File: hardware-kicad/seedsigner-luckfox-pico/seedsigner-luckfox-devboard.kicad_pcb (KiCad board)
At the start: 2 copper layers, 100 x 100 mm, 37 parts, among them J1 Conn_01x10, J2 Conn_01x05, U1 LuckFox_Pico, U2 RASPBERRY_PI_3_MODEL_B+

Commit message: export footprint library pretty files, and update pcb to use library
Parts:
- ART1: footprint SeedSigner:LightningSpore_Logo -> seedsigner-luckfox:LightningSpore_Logo
- C1: footprint Capacitor_THT:CP_Radial_D5.0mm_P2.50mm -> seedsigner-luckfox:CP_Radial_D5.0mm_P2.50mm
- H1, H2, H3, H4: footprint SeedSigner:MOUNT_HOLE_3MM -> seedsigner-luckfox:MOUNT_HOLE_3MM
- J1: footprint Connector_PinHeader_2.54mm:PinHeader_1x10_P2.54mm_Horizontal -> seedsigner-luckfox:PinHeader_1x10_P2.54mm_Horizontal
- J2: footprint Connector_PinHeader_2.54mm:PinHeader_1x05_P2.54mm_Horizontal -> seedsigner-luckfox:PinHeader_1x05_P2.54mm_Horizontal
- JP1: footprint Jumper:SolderJumper-2_P1.3mm_Bridged_Pad1.0x1.5mm -> seedsigner-luckfox:SolderJumper-2_P1.3mm_Bridged_Pad1.0x1.5mm
- JP2: footprint Jumper:SolderJumper-2_P1.3mm_Open_Pad1.0x1.5mm -> seedsigner-luckfox:SolderJumper-2_P1.3mm_Open_Pad1.0x1.5mm
- LOGO1: footprint SeedSigner:seedsigner-logo-small -> seedsigner-luckfox:seedsigner-logo-small
- LOGO2: footprint SeedSigner:corn-logo -> seedsigner-luckfox:corn-logo
- R1, R2, R3, R4, R5, R6, R7, R8: footprint Resistor_SMD:R_2512_6332Metric -> seedsigner-luckfox:R_2512_6332Metric
- TP1, TP10, TP11, TP12, TP13, TP14, TP15, TP2, TP3, TP4, TP5, TP6, TP7, TP8, TP9: footprint TestPoint:TestPoint_Pad_1.5x1.5mm -> seedsigner-luckfox:TestPoint_Pad_1.5x1.5mm
- U1: footprint SeedSigner:LUCKFOX_PICO_PRO_MAX_PTH -> seedsigner-luckfox:LUCKFOX_PICO_PRO_MAX_PTH
- U2: footprint SeedSigner:WAVESHARE_LCD_BUTTON -> seedsigner-luckfox:WAVESHARE_LCD_BUTTON
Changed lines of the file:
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@@
 	(net 54 "Net-(U1-GPIO4_C1_z)")
 	(net 55 "Net-(U1-GPIO0_A7_d)")
-	(footprint "TestPoint:TestPoint_Pad_1.5x1.5mm"
+	(footprint "seedsigner-luckfox:TestPoint_Pad_1.5x1.5mm"
 		(layer "F.Cu")
 		(at 59 15)
@@
 		)
 	)
-	(footprint "Resistor_SMD:R_2512_6332Metric"
+	(footprint "seedsigner-luckfox:R_2512_6332Metric"
 		(layer "F.Cu")
 		(at 17.8 50.2375 90)
@@
 		)
 	)
-	(footprint "TestPoint:TestPoint_Pad_1.5x1.5mm"
+	(footprint "seedsigner-luckfox:TestPoint_Pad_1.5x1.5mm"
 		(layer "F.Cu")
 		(at 40.75 15)
@@
 		)
 	)
-	(footprint "Capacitor_THT:CP_Radial_D5.0mm_P2.50mm"
+	(footprint "seedsigner-luckfox:CP_Radial_D5.0mm_P2.50mm"
 		(layer "F.Cu")
 		(at 71 53 180)
@@
 		)
 	)
-	(footprint "Resistor_SMD:R_2512_6332Metric"
+	(footprint "seedsigner-luckfox:R_2512_6332Metric"
 		(layer "F.Cu")
 		(at 32.2 50.2 90)
@@
 		)
 	)
-	(footprint "TestPoint:TestPoint_Pad_1.5x1.5mm"
+	(footprint "seedsigner-luckfox:TestPoint_Pad_1.5x1.5mm"
 		(layer "F.Cu")
 		(at 6.25 13.75)
@@
 		)
 	)
-	(footprint "SeedSigner:LightningSpore_Logo"
+	(footprint "seedsigner-luckfox:LightningSpore_Logo"
 		(layer "F.Cu")
 		(at 94.85827 53.012464 90)
@@
 		)
 	)
-	(footprint "SeedSigner:seedsigner-logo-small"
+	(footprint "seedsigner-luckfox:seedsigner-logo-small"
 		(layer "F.Cu")
 		(at 95.175 20.875 90)
@@
 		)
 	)
-	(footprint "Resistor_SMD:R_2512_6332Metric"
+	(footprint "seedsigner-luckfox:R_2512_6332Metric"
 		(layer "F.Cu")
 		(at 22.6 50.2 90)
@@
 		)
 	)
-	(footprint "Resistor_SMD:R_2512_6332Metric"
+	(footprint "seedsigner-luckfox:R_2512_6332Metric"
 		(layer "F.Cu")
 		(at 47 50.1625 90)
@@
 		)
 	)
-	(footprint "TestPoint:TestPoint_Pad_1.5x1.5mm"
+	(footprint "seedsigner-luckfox:TestPoint_Pad_1.5x1.5mm"
 		(layer "F.Cu")
 		(at 48.5 15)
@@
 		)
 	)
-	(footprint "Connector_PinHeader_2.54mm:PinHeader_1x05_P2.54mm_Horizontal"
+	(footprint "seedsigner-luckfox:PinHeader_1x05_P2.54mm_Horizontal"
 		(layer "F.Cu")
 		(at 63.675 11.375 90)
@@
 		)
 	)
-	(footprint "TestPoint:TestPoint_Pad_1.5x1.5mm"
+	(footprint "seedsigner-luckfox:TestPoint_Pad_1.5x1.5mm"
 		(layer "F.Cu")
 		(at 6.25 26.25)
@@
 		)
 	)
-	(footprint "TestPoint:TestPoint_Pad_1.5x1.5mm"
+	(footprint "seedsigner-luckfox:TestPoint_Pad_1.5x1.5mm"
 		(layer "F.Cu")
 		(at 55.75 41.5)
@@
 		)
 	)
-	(footprint "SeedSigner:MOUNT_HOLE_3MM"
+	(footprint "seedsigner-luckfox:MOUNT_HOLE_3MM"
 		(layer "F.Cu")
 		(at 95 5)
@@
 		)
 	)
-	(footprint "TestPoint:TestPoint_Pad_1.5x1.5mm"
+	(footprint "seedsigner-luckfox:TestPoint_Pad_1.5x1.5mm"
 		(layer "F.Cu")
 		(at 51.5 15)
@@
 		)
 	)
-	(footprint "Jumper:SolderJumper-2_P1.3mm_Open_Pad1.0x1.5mm"
+	(footprint "seedsigner-luckfox:SolderJumper-2_P1.3mm_Open_Pad1.0x1.5mm"
 		(layer "F.Cu")
 		(at 77.65 61.7 180)
@@
 		)
 	)
-	(footprint "Resistor_SMD:R_2512_6332Metric"
+	(footprint "seedsigner-luckfox:R_2512_6332Metric"
 		(layer "F.Cu")
 		(at 42 50.2 90)
@@
 		)
 	)
-	(footprint "TestPoint:TestPoint_Pad_1.5x1.5mm"
+	(footprint "seedsigner-luckfox:TestPoint_Pad_1.5x1.5mm"
 		(layer "F.Cu")
 		(at 54.25 15)
@@
 		)
 	)
-	(footprint "SeedSigner:WAVESHARE_LCD_BUTTON"
+	(footprint "seedsigner-luckfox:WAVESHARE_LCD_BUTTON"
 		(layer "F.Cu")
 		(at 49 83.8 180)
@@
 		)
 	)
-	(footprint "Resistor_SMD:R_2512_6332Metric"
+	(footprint "seedsigner-luckfox:R_2512_6332Metric"
 		(layer "F.Cu")
 		(at 27.4 50.2 90)
@@
 		)
 	)
-	(footprint "SeedSigner:MOUNT_HOLE_3MM"
+	(footprint "seedsigner-luckfox:MOUNT_HOLE_3MM"
 		(layer "F.Cu")
 		(at 95 95)
@@
 		)
 	)
-	(footprint "TestPoint:TestPoint_Pad_1.5x1.5mm"
+	(footprint "seedsigner-luckfox:TestPoint_Pad_1.5x1.5mm"
 		(layer "F.Cu")
 		(at 38.25 15)
@@
 		)
 	)
-	(footprint "SeedSigner:LUCKFOX_PICO_PRO_MAX_PTH"
+	(footprint "seedsigner-luckfox:LUCKFOX_PICO_PRO_MAX_PTH"
 		(layer "F.Cu")
 		(at 17.86 36.5 90)
@@
 		)
 	)
-	(footprint "SeedSigner:corn-logo"
+	(footprint "seedsigner-luckfox:corn-logo"
 		(layer "F.Cu")
 		(at 93.056841 83.1 90)
@@
 		)
 	)
-	(footprint "Resistor_SMD:R_2512_6332Metric"
+	(footprint "seedsigner-luckfox:R_2512_6332Metric"
 		(layer "F.Cu")
 		(at 37 50.2 90)
@@
 		)
 	)
-	(footprint "TestPoint:TestPoint_Pad_1.5x1.5mm"
+	(footprint "seedsigner-luckfox:TestPoint_Pad_1.5x1.5mm"
 		(layer "F.Cu")
 		(at 6.25 17.75)
@@
 		)
 	)
-	(footprint "TestPoint:TestPoint_Pad_1.5x1.5mm"
+	(footprint "seedsigner-luckfox:TestPoint_Pad_1.5x1.5mm"
 		(layer "F.Cu")
 		(at 33.25 15)
@@
 		)
 	)
-	(footprint "TestPoint:TestPoint_Pad_1.5x1.5mm"
+	(footprint "seedsigner-luckfox:TestPoint_Pad_1.5x1.5mm"
 		(layer "F.Cu")
 		(at 61.75 15)
@@
 		)
 	)
-	(footprint "Jumper:SolderJumper-2_P1.3mm_Bridged_Pad1.0x1.5mm"
+	(footprint "seedsigner-luckfox:SolderJumper-2_P1.3mm_Bridged_Pad1.0x1.5mm"
 		(layer "F.Cu")
 		(at 74.15 61.7)
@@
 		)
 	)
-	(footprint "Connector_PinHeader_2.54mm:PinHeader_1x10_P2.54mm_Horizontal"
+	(footprint "seedsigner-luckfox:PinHeader_1x10_P2.54mm_Horizontal"
 		(layer "F.Cu")
 		(at 10 77.5 180)
@@
 		)
 	)
-	(footprint "TestPoint:TestPoint_Pad_1.5x1.5mm"
+	(footprint "seedsigner-luckfox:TestPoint_Pad_1.5x1.5mm"
 		(layer "F.Cu")
 		(at 6.25 22)
@@
 		)
 	)
-	(footprint "SeedSigner:MOUNT_HOLE_3MM"
+	(footprint "seedsigner-luckfox:MOUNT_HOLE_3MM"
 		(layer "F.Cu")
 		(at 5 5)
@@
 		)
 	)
-	(footprint "TestPoint:TestPoint_Pad_1.5x1.5mm"
+	(footprint "seedsigner-luckfox:TestPoint_Pad_1.5x1.5mm"
 		(layer "F.Cu")
 		(at 44.75 15)
@@
 		)
 	)
-	(footprint "TestPoint:TestPoint_Pad_1.5x1.5mm"
+	(footprint "seedsigner-luckfox:TestPoint_Pad_1.5x1.5mm"
 		(layer "F.Cu")
 		(at 56.5 15)
@@
 		)
 	)
-	(footprint "SeedSigner:MOUNT_HOLE_3MM"
+	(footprint "seedsigner-luckfox:MOUNT_HOLE_3MM"
 		(layer "F.Cu")
 		(at 5 95)
@@
 		)
 	)
-	(footprint "Resistor_SMD:R_2512_6332Metric"
+	(footprint "seedsigner-luckfox:R_2512_6332Metric"
 		(layer "F.Cu")
 		(at 51.8 50.2 90)

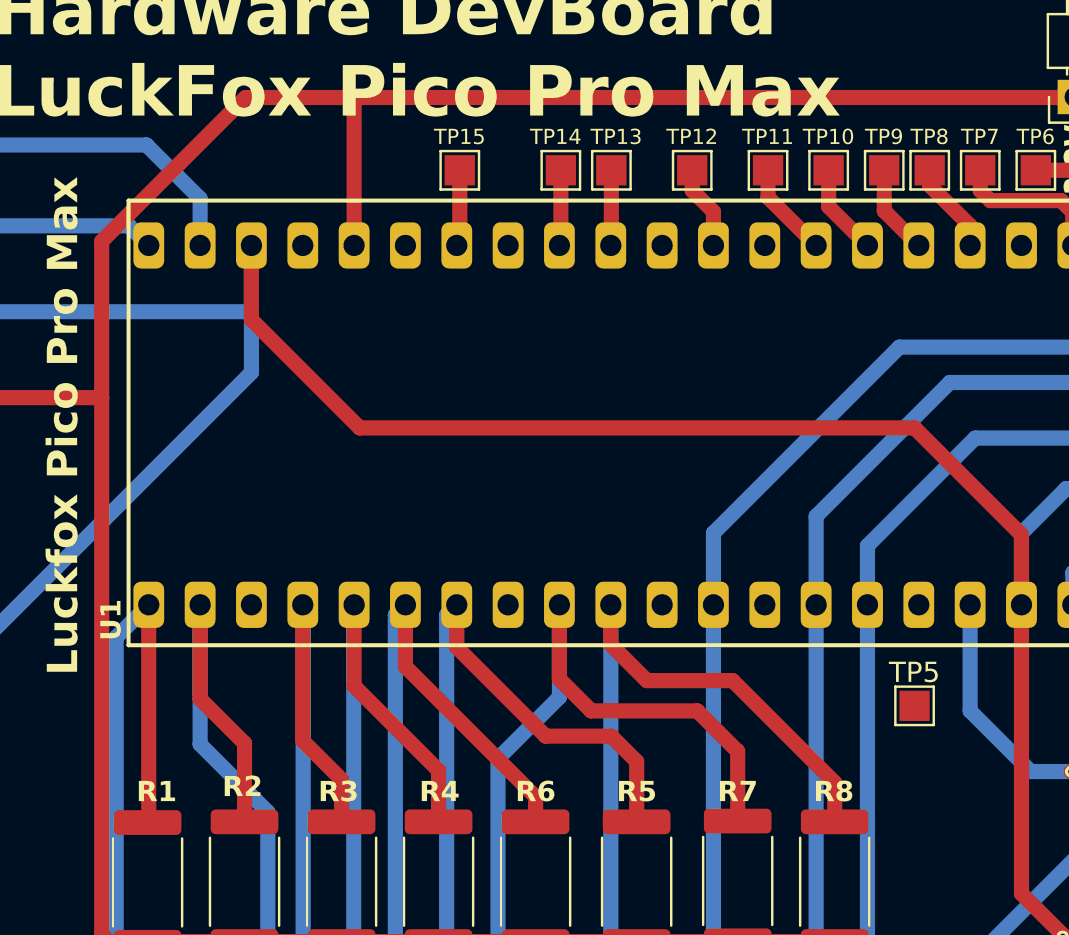
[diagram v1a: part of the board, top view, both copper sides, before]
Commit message: update libraries and make schematic and pcb only use parts from library
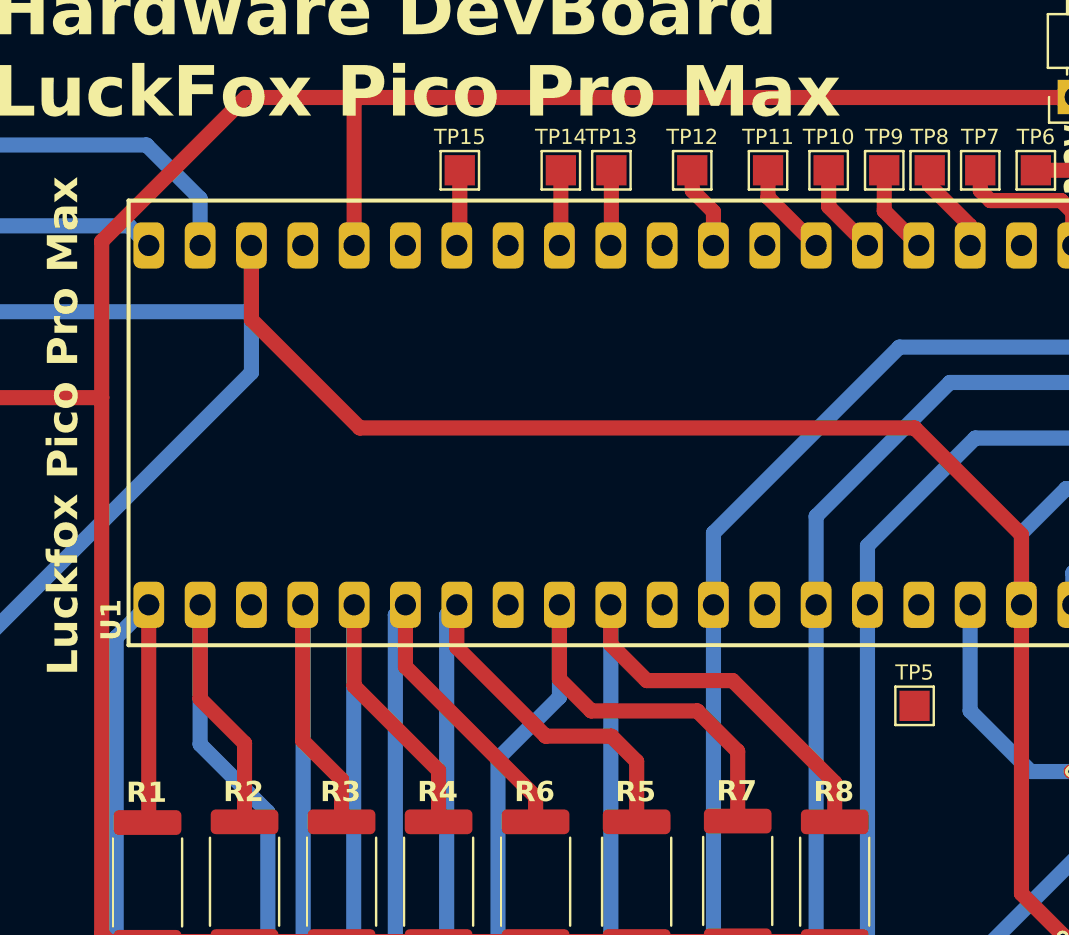
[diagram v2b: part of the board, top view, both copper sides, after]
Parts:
- U1: value LuckFox_Pico -> LuckFox_Pico_PLUS_PRO
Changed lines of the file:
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@@
 			)
 		)
-		(property "Footprint" "TestPoint:TestPoint_Pad_1.5x1.5mm"
+		(property "Footprint" "seedsigner-luckfox:TestPoint_Pad_1.5x1.5mm"
 			(at 0 0 0)
 			(unlocked yes)
@@
 		(tags "resistor")
 		(property "Reference" "R1"
-			(at 4.4875 0.45 180)
+			(at 4.45 -0.05 180)
 			(layer "F.SilkS")
 			(effects
@@
 			)
 		)
-		(property "Footprint" "Resistor_SMD:R_2512_6332Metric"
+		(property "Footprint" "seedsigner-luckfox:R_2512_6332Metric"
 			(at 0 0 90)
 			(unlocked yes)
@@
 		(tags "test point SMD pad rectangle square")
 		(property "Reference" "TP13"
-			(at 0.25 -1.648 0)
+			(at 0 -1.648 0)
 			(layer "F.SilkS")
 			(effects
@@
 			)
 		)
-		(property "Footprint" "TestPoint:TestPoint_Pad_1.5x1.5mm"
+		(property "Footprint" "seedsigner-luckfox:TestPoint_Pad_1.5x1.5mm"
 			(at 0 0 0)
 			(unlocked yes)
@@
 			)
 		)
-		(property "Footprint" "Capacitor_THT:CP_Radial_D5.0mm_P2.50mm"
+		(property "Footprint" "seedsigner-luckfox:CP_Radial_D5.0mm_P2.50mm"
 			(at 0 0 180)
 			(unlocked yes)
@@
 		(tags "resistor")
 		(property "Reference" "R4"
-			(at 4.45 0.05 180)
+			(at 4.45 -0.05 180)
 			(layer "F.SilkS")
 			(effects
@@
 			)
 		)
-		(property "Footprint" "Resistor_SMD:R_2512_6332Metric"
+		(property "Footprint" "seedsigner-luckfox:R_2512_6332Metric"
 			(at 0 0 90)
 			(unlocked yes)
@@
 			)
 		)
-		(property "Footprint" "TestPoint:TestPoint_Pad_1.5x1.5mm"
+		(property "Footprint" "seedsigner-luckfox:TestPoint_Pad_1.5x1.5mm"
 			(at 0 0 0)
 			(unlocked yes)
@@
 			)
 		)
-		(property "Footprint" "SeedSigner:LightningSpore_Logo"
+		(property "Footprint" "seedsigner-luckfox:LightningSpore_Logo"
 			(at 0 0 90)
 			(unlocked yes)
@@
 			)
 		)
-		(property "Footprint" "SeedSigner:seedsigner-logo-small"
+		(property "Footprint" "seedsigner-luckfox:seedsigner-logo-small"
 			(at 0 0 90)
 			(layer "F.Fab")
@@
 		(tags "resistor")
 		(property "Reference" "R2"
-			(at 4.7 -0.1 180)
+			(at 4.45 -0.05 180)
 			(layer "F.SilkS")
 			(effects
@@
 			)
 		)
-		(property "Footprint" "Resistor_SMD:R_2512_6332Metric"
+		(property "Footprint" "seedsigner-luckfox:R_2512_6332Metric"
 			(at 0 0 90)
 			(unlocked yes)
@@
 		(tags "resistor")
 		(property "Reference" "R7"
-			(at 4.4125 0 180)
+			(at 4.45 -0.05 180)
 			(layer "F.SilkS")
 			(effects
@@
 			)
 		)
-		(property "Footprint" "Resistor_SMD:R_2512_6332Metric"
+		(property "Footprint" "seedsigner-luckfox:R_2512_6332Metric"
 			(at 0 0 90)
 			(unlocked yes)
@@
 			)
 		)
-		(property "Footprint" "TestPoint:TestPoint_Pad_1.5x1.5mm"
+		(property "Footprint" "seedsigner-luckfox:TestPoint_Pad_1.5x1.5mm"
 			(at 0 0 0)
 			(unlocked yes)
@@
 			)
 		)
-		(property "Footprint" "Connector_PinHeader_2.54mm:PinHeader_1x05_P2.54mm_Horizontal"
+		(property "Footprint" "seedsigner-luckfox:PinHeader_1x05_P2.54mm_Horizontal"
 			(at 0 0 90)
 			(unlocked yes)
@@
 			)
 		)
-		(property "Footprint" "TestPoint:TestPoint_Pad_1.5x1.5mm"
+		(property "Footprint" "seedsigner-luckfox:TestPoint_Pad_1.5x1.5mm"
 			(at 0 0 0)
 			(unlocked yes)
@@
 			(effects
 				(font
-					(size 1 1)
+					(size 0.75 0.75)
 					(thickness 0.15)
 				)
@@
 			)
 		)
-		(property "Footprint" "TestPoint:TestPoint_Pad_1.5x1.5mm"
+		(property "Footprint" "seedsigner-luckfox:TestPoint_Pad_1.5x1.5mm"
 			(at 0 0 0)
 			(unlocked yes)
@@
 			)
 		)
-		(property "Footprint" "SeedSigner:MOUNT_HOLE_3MM"
+		(property "Footprint" "seedsigner-luckfox:MOUNT_HOLE_3MM"
 			(at 0 0 0)
 			(layer "F.Fab")
@@
 			)
 		)
-		(property "Footprint" "TestPoint:TestPoint_Pad_1.5x1.5mm"
+		(property "Footprint" "seedsigner-luckfox:TestPoint_Pad_1.5x1.5mm"
 			(at 0 0 0)
 			(unlocked yes)
@@
 			)
 		)
-		(property "Footprint" "Jumper:SolderJumper-2_P1.3mm_Open_Pad1.0x1.5mm"
+		(property "Footprint" "seedsigner-luckfox:SolderJumper-2_P1.3mm_Open_Pad1.0x1.5mm"
 			(at 0 0 180)
 			(unlocked yes)
@@
 		(tags "resistor")
 		(property "Reference" "R5"
-			(at 4.45 0 180)
+			(at 4.45 -0.05 180)
 			(layer "F.SilkS")
 			(effects
@@
 			)
 		)
-		(property "Footprint" "Resistor_SMD:R_2512_6332Metric"
+		(property "Footprint" "seedsigner-luckfox:R_2512_6332Metric"
 			(at 0 0 90)
 			(unlocked yes)
@@
 			)
 		)
-		(property "Footprint" "TestPoint:TestPoint_Pad_1.5x1.5mm"
+		(property "Footprint" "seedsigner-luckfox:TestPoint_Pad_1.5x1.5mm"
 			(at 0 0 0)
 			(unlocked yes)
@@
 			)
 		)
-		(property "Footprint" "SeedSigner:WAVESHARE_LCD_BUTTON"
+		(property "Footprint" "seedsigner-luckfox:WAVESHARE_LCD_BUTTON"
 			(at 0 0 0)
 			(layer "F.Fab")
@@
 		(tags "resistor")
 		(property "Reference" "R3"
-			(at 4.45 -0.15 180)
+			(at 4.45 -0.05 180)
 			(layer "F.SilkS")
 			(effects
@@
 			)
 		)
-		(property "Footprint" "Resistor_SMD:R_2512_6332Metric"
+		(property "Footprint" "seedsigner-luckfox:R_2512_6332Metric"
 			(at 0 0 90)
 			(unlocked yes)
@@
 			)
 		)
-		(property "Footprint" "SeedSigner:MOUNT_HOLE_3MM"
+		(property "Footprint" "seedsigner-luckfox:MOUNT_HOLE_3MM"
 			(at 0 0 0)
 			(layer "F.Fab")
@@
 		(tags "test point SMD pad rectangle square")
 		(property "Reference" "TP14"
-			(at -0.25 -1.648 0)
+			(at 0 -1.648 0)
 			(layer "F.SilkS")
 			(effects
@@
 			)
 		)
-		(property "Footprint" "TestPoint:TestPoint_Pad_1.5x1.5mm"
+		(property "Footprint" "seedsigner-luckfox:TestPoint_Pad_1.5x1.5mm"
 			(at 0 0 0)
 			(unlocked yes)
@@
 			)
 		)
-		(property "Value" "LuckFox_Pico"
+		(property "Value" "LuckFox_Pico_PLUS_PRO"
 			(at 22.86 -17.78 90)
 			(unlocked yes)
@@
 			)
 		)
-		(property "Footprint" "SeedSigner:LUCKFOX_PICO_PRO_MAX_PTH"
+		(property "Footprint" "seedsigner-luckfox:LUCKFOX_PICO_PRO_MAX_PTH"
 			(at 0 0 90)
 			(unlocked yes)
@@
 			)
 		)
-		(property "Footprint" "SeedSigner:corn-logo"
+		(property "Footprint" "seedsigner-luckfox:corn-logo"
 			(at 0 0 90)
 			(layer "F.Fab")
@@
 		(tags "resistor")
 		(property "Reference" "R6"
-			(at 4.45 0 180)
+			(at 4.45 -0.05 180)
 			(layer "F.SilkS")
 			(effects
@@
 			)
 		)
-		(property "Footprint" "Resistor_SMD:R_2512_6332Metric"
+		(property "Footprint" "seedsigner-luckfox:R_2512_6332Metric"
 			(at 0 0 90)
 			(unlocked yes)
@@
 			)
 		)
-		(property "Footprint" "TestPoint:TestPoint_Pad_1.5x1.5mm"
+		(property "Footprint" "seedsigner-luckfox:TestPoint_Pad_1.5x1.5mm"
 			(at 0 0 0)
 			(unlocked yes)
@@
 			)
 		)
-		(property "Footprint" "TestPoint:TestPoint_Pad_1.5x1.5mm"
+		(property "Footprint" "seedsigner-luckfox:TestPoint_Pad_1.5x1.5mm"
 			(at 0 0 0)
 			(unlocked yes)
@@
 			)
 		)
-		(property "Footprint" "TestPoint:TestPoint_Pad_1.5x1.5mm"
+		(property "Footprint" "seedsigner-luckfox:TestPoint_Pad_1.5x1.5mm"
 			(at 0 0 0)
 			(unlocked yes)
@@
 			)
 		)
-		(property "Footprint" "Jumper:SolderJumper-2_P1.3mm_Bridged_Pad1.0x1.5mm"
+		(property "Footprint" "seedsigner-luckfox:SolderJumper-2_P1.3mm_Bridged_Pad1.0x1.5mm"
 			(at 0 0 0)
 			(unlocked yes)
@@
 			)
 		)
-		(property "Footprint" "Connector_PinHeader_2.54mm:PinHeader_1x10_P2.54mm_Horizontal"
+		(property "Footprint" "seedsigner-luckfox:PinHeader_1x10_P2.54mm_Horizontal"
 			(at 0 0 180)
 			(unlocked yes)
@@
 			)
 		)
-		(property "Footprint" "TestPoint:TestPoint_Pad_1.5x1.5mm"
+		(property "Footprint" "seedsigner-luckfox:TestPoint_Pad_1.5x1.5mm"
 			(at 0 0 0)
 			(unlocked yes)
@@
 			)
 		)
-		(property "Footprint" "SeedSigner:MOUNT_HOLE_3MM"
+		(property "Footprint" "seedsigner-luckfox:MOUNT_HOLE_3MM"
 			(at 0 0 0)
 			(layer "F.Fab")
@@
 			)
 		)
-		(property "Footprint" "TestPoint:TestPoint_Pad_1.5x1.5mm"
+		(property "Footprint" "seedsigner-luckfox:TestPoint_Pad_1.5x1.5mm"
 			(at 0 0 0)
 			(unlocked yes)
@@
 			)
 		)
-		(property "Footprint" "TestPoint:TestPoint_Pad_1.5x1.5mm"
+		(property "Footprint" "seedsigner-luckfox:TestPoint_Pad_1.5x1.5mm"
 			(at 0 0 0)
 			(unlocked yes)
@@
 			)
 		)
-		(property "Footprint" "SeedSigner:MOUNT_HOLE_3MM"
+		(property "Footprint" "seedsigner-luckfox:MOUNT_HOLE_3MM"
 			(at 0 0 0)
 			(layer "F.Fab")
@@
 			)
 		)
-		(property "Footprint" "Resistor_SMD:R_2512_6332Metric"
+		(property "Footprint" "seedsigner-luckfox:R_2512_6332Metric"
 			(at 0 0 90)
 			(unlocked yes)
